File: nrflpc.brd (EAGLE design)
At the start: 67.9 x 38.8 mm, 55 parts, among them IC1 LPC1111/12/13/14-HVQFN33, IC3 LM3401, IC5 LM3401, IC6 LM3401, IC7 LM3401, IC8 78L05SMD, Q2 MOSFET-PCHANNEL, Q3 MOSFET-PCHANNEL, Q4 MOSFET-PCHANNEL, Q5 MOSFET-PCHANNEL

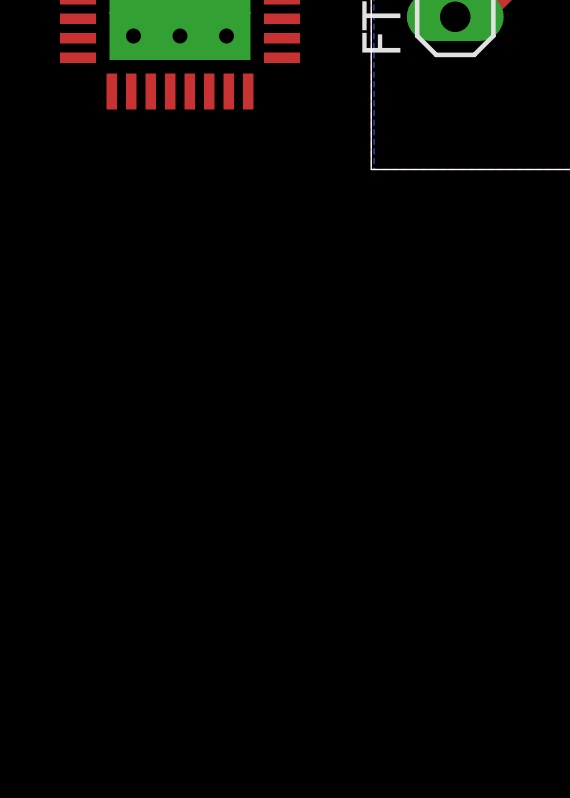
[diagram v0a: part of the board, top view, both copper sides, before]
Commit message: Basic LPC circuitry for crystal and power
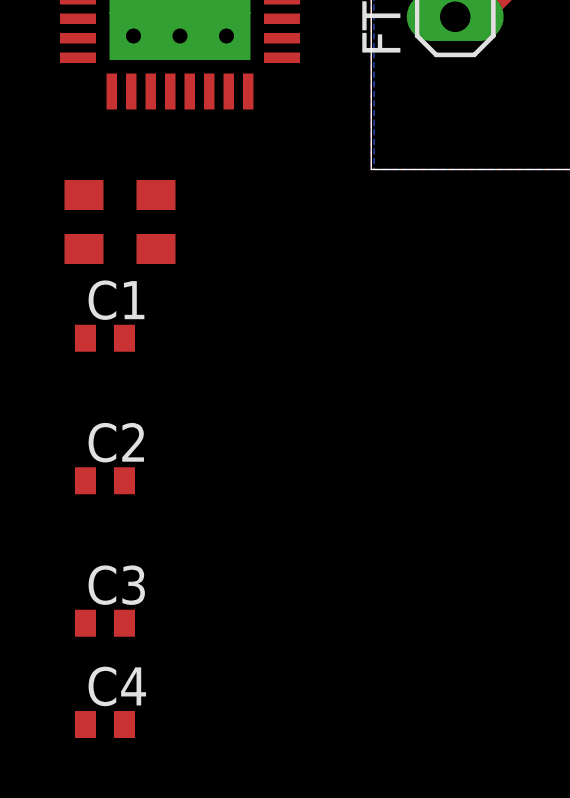
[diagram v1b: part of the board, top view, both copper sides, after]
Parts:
- added C1, C2: 18pF, rcl:C0402
- added C3, C4: 100nF, rcl:C0402
- added Q1: 20MHz, seb:MT
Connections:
- removed net VDD1: IC1.29
- removed net VDD2: IC1.6
- removed net VSS: IC1.33
- new net N$19: C2.2, IC1.4, Q1.3
- new net N$29: C1.1, IC1.5, Q1.1
- net +3V3: now also C3.1, C4.1, IC1.29, IC1.6
- net GND: now also C1.2, C2.1, C3.2, C4.2, IC1.33
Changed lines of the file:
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@@
 <element name="EXT" library="pinhead" package="2X05" value="" x="63.3" y="8.4" rot="R270"/>
 <element name="IC1" library="lpc1100v1.1" package="HVQFN33" value="LPC1111/12/13/14-HVQFN33" x="-6.375" y="6"/>
+<element name="Q1" library="seb" package="MT" value="20MHz" x="-8.375" y="-1.75"/>
+<element name="C1" library="rcl" package="C0402" value="18pF" x="-8.875" y="-5.625"/>
+<element name="C2" library="rcl" package="C0402" value="18pF" x="-8.875" y="-10.375"/>
+<element name="C3" library="rcl" package="C0402" value="100nF" x="-8.875" y="-15.125"/>
+<element name="C4" library="rcl" package="C0402" value="100nF" x="-8.875" y="-18.5"/>
 </elements>
 <signals>
@@
 <vertex x="0" y="0"/>
 </polygon>
+<contactref element="C2" pad="1"/>
+<contactref element="C1" pad="2"/>
+<contactref element="IC1" pad="33"/>
+<contactref element="C4" pad="2"/>
+<contactref element="C3" pad="2"/>
 <wire x1="52.178" y1="32.8" x2="57.66" y2="33.496" width="0" layer="19" extent="1-1"/>
 <wire x1="50.252" y1="32.743" x2="52.178" y2="32.8" width="0" layer="19" extent="1-1"/>
@@
 <wire x1="51.27" y1="3.99" x2="44" y2="6.965" width="0" layer="19" extent="1-1"/>
 <wire x1="65.052" y1="27.143" x2="57.66" y2="33.496" width="0" layer="19" extent="1-1"/>
+<wire x1="-6.375" y1="6" x2="2.8" y2="12.71" width="0" layer="19" extent="1-1"/>
+<wire x1="-8.225" y1="-5.625" x2="-6.375" y2="6" width="0" layer="19" extent="1-1"/>
+<wire x1="-9.525" y1="-10.375" x2="-8.225" y2="-5.625" width="0" layer="19" extent="1-1"/>
+<wire x1="-8.225" y1="-15.125" x2="-9.525" y2="-10.375" width="0" layer="19" extent="1-1"/>
+<wire x1="-8.225" y1="-18.5" x2="-8.225" y2="-15.125" width="0" layer="19" extent="1-1"/>
 <wire x1="64.57" y1="3.32" x2="51.27" y2="3.99" width="0" layer="19" extent="1-1"/>
 </signal>
@@
 <contactref element="JP1" pad="2"/>
 <contactref element="EXT" pad="1"/>
+<contactref element="IC1" pad="29"/>
+<contactref element="IC1" pad="6"/>
+<contactref element="C3" pad="1"/>
+<contactref element="C4" pad="1"/>
 <wire x1="48.73" y1="3.99" x2="62.03" y2="13.48" width="0" layer="19" extent="1-1"/>
 <wire x1="43.95" y1="4" x2="48.73" y2="3.99" width="0" layer="19" extent="1-1"/>
 <wire x1="44" y1="5.695" x2="43.95" y2="4" width="0" layer="19" extent="1-1"/>
+<wire x1="-6.7" y1="9.4" x2="44" y2="5.695" width="0" layer="19" extent="1-1"/>
+<wire x1="-9.775" y1="5.025" x2="-6.7" y2="9.4" width="0" layer="19" extent="1-1"/>
+<wire x1="-9.525" y1="-15.125" x2="-9.775" y2="5.025" width="0" layer="19" extent="1-1"/>
+<wire x1="-9.525" y1="-18.5" x2="-9.525" y2="-15.125" width="0" layer="19" extent="1-1"/>
 </signal>
 <signal name="CE">
@@
 <signal name="IO2">
 <contactref element="EXT" pad="9"/>
-</signal>
-<signal name="VDD1">
-<contactref element="IC1" pad="29"/>
-</signal>
-<signal name="VDD2">
-<contactref element="IC1" pad="6"/>
-</signal>
-<signal name="VSS">
-<contactref element="IC1" pad="33"/>
 </signal>
 <signal name="N$18">
@@
 <wire x1="40.7" y1="4" x2="38.8" y2="5.695" width="0" layer="19" extent="1-1"/>
 </signal>
+<signal name="N$19">
+<contactref element="IC1" pad="4"/>
+<contactref element="Q1" pad="3"/>
+<contactref element="C2" pad="2"/>
+<wire x1="-9.575" y1="-2.65" x2="-8.225" y2="-10.375" width="0" layer="19" extent="1-1"/>
+<wire x1="-9.775" y1="6.325" x2="-9.575" y2="-2.65" width="0" layer="19" extent="1-1"/>
+</signal>
+<signal name="N$29">
+<contactref element="IC1" pad="5"/>
+<contactref element="Q1" pad="1"/>
+<contactref element="C1" pad="1"/>
+<wire x1="-7.175" y1="-0.85" x2="-9.525" y2="-5.625" width="0" layer="19" extent="1-1"/>
+<wire x1="-9.775" y1="5.675" x2="-7.175" y2="-0.85" width="0" layer="19" extent="1-1"/>
+</signal>
 </signals>

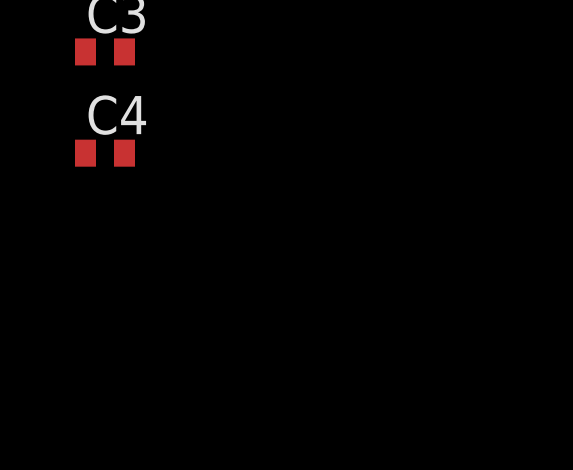
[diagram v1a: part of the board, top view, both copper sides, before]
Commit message: Chosen good fitting PWM Pins, Reset circuitry
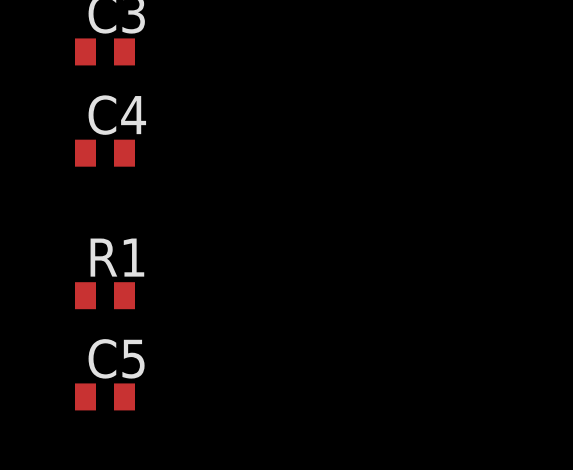
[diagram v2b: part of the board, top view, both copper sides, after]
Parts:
- added C5: 100nF, rcl:C0402
- added R1: (no value), rcl:R0402
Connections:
- net !RST: now also C5.1, IC1.2, R1.1
- net +3V3: now also R1.2
- net GND: now also C5.2
- net PB: now also IC1.25
- net PG: now also IC1.31
- net PR: now also IC1.32
- net PW: now also IC1.24
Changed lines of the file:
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@@
 <element name="C3" library="rcl" package="C0402" value="100nF" x="-8.875" y="-15.125"/>
 <element name="C4" library="rcl" package="C0402" value="100nF" x="-8.875" y="-18.5"/>
+<element name="R1" library="rcl" package="R0402" value="" x="-8.875" y="-23.25"/>
+<element name="C5" library="rcl" package="C0402" value="100nF" x="-8.875" y="-26.625"/>
 </elements>
 <signals>
@@
 <wire x1="24.25" y1="11.25" x2="25.5" y2="10" width="0.4064" layer="16"/>
 <wire x1="25.5" y1="10" x2="28.1" y2="10" width="0.4064" layer="16"/>
+<contactref element="R1" pad="1"/>
+<contactref element="C5" pad="1"/>
+<contactref element="IC1" pad="2"/>
+<wire x1="-9.525" y1="-23.25" x2="-9.525" y2="-26.625" width="0" layer="19" extent="1-1"/>
+<wire x1="-9.775" y1="7.625" x2="-9.525" y2="-23.25" width="0" layer="19" extent="1-1"/>
+<wire x1="2.8" y1="5.09" x2="-9.775" y2="7.625" width="0" layer="19" extent="1-1"/>
 </signal>
 <signal name="RXD">
@@
 <wire x1="30.3" y1="17.6" x2="35.849" y2="17.6" width="0.4064" layer="1"/>
 <wire x1="35.849" y1="17.6" x2="35.849" y2="19.0205" width="0.4064" layer="1"/>
+<contactref element="IC1" pad="25"/>
+<wire x1="-4.1" y1="9.4" x2="30.3" y2="13.0666" width="0" layer="19" extent="1-1"/>
 </signal>
 <signal name="PG">
@@
 <wire x1="19.649" y1="17.9615" x2="21.8385" y2="17.9615" width="0.4064" layer="1"/>
 <wire x1="21.8385" y1="17.9615" x2="22.2" y2="17.6" width="0.4064" layer="1"/>
+<contactref element="IC1" pad="31"/>
+<wire x1="-8" y1="9.4" x2="19.5" y2="18.1105" width="0" layer="19" extent="1-1"/>
 </signal>
 <signal name="PR">
@@
 <wire x1="5.9" y1="19.6" x2="5.9" y2="22.3" width="0.4064" layer="1"/>
 <wire x1="5.9" y1="22.3" x2="8.025" y2="24.425" width="0.4064" layer="1"/>
+<contactref element="IC1" pad="32"/>
+<wire x1="-8.65" y1="9.4" x2="5.149" y2="17.4865" width="0" layer="19" extent="1-1"/>
 </signal>
 <signal name="PW">
@@
 <wire x1="51.9" y1="16.695" x2="53.803" y2="16.695" width="0.4064" layer="1"/>
 <wire x1="53.803" y1="16.695" x2="53.803" y2="17.634" width="0.4064" layer="1"/>
+<contactref element="IC1" pad="24"/>
+<wire x1="-2.975" y1="8.275" x2="30.995" y2="16.695" width="0" layer="19" extent="1-1"/>
 </signal>
 <signal name="+12V">
@@
 <contactref element="C4" pad="2"/>
 <contactref element="C3" pad="2"/>
+<contactref element="C5" pad="2"/>
 <wire x1="52.178" y1="32.8" x2="57.66" y2="33.496" width="0" layer="19" extent="1-1"/>
 <wire x1="50.252" y1="32.743" x2="52.178" y2="32.8" width="0" layer="19" extent="1-1"/>
@@
 <wire x1="-8.225" y1="-15.125" x2="-9.525" y2="-10.375" width="0" layer="19" extent="1-1"/>
 <wire x1="-8.225" y1="-18.5" x2="-8.225" y2="-15.125" width="0" layer="19" extent="1-1"/>
+<wire x1="-8.225" y1="-26.625" x2="-8.225" y2="-18.5" width="0" layer="19" extent="1-1"/>
 <wire x1="64.57" y1="3.32" x2="51.27" y2="3.99" width="0" layer="19" extent="1-1"/>
 </signal>
@@
 <contactref element="C3" pad="1"/>
 <contactref element="C4" pad="1"/>
+<contactref element="R1" pad="2"/>
 <wire x1="48.73" y1="3.99" x2="62.03" y2="13.48" width="0" layer="19" extent="1-1"/>
 <wire x1="43.95" y1="4" x2="48.73" y2="3.99" width="0" layer="19" extent="1-1"/>
@@
 <wire x1="-9.525" y1="-15.125" x2="-9.775" y2="5.025" width="0" layer="19" extent="1-1"/>
 <wire x1="-9.525" y1="-18.5" x2="-9.525" y2="-15.125" width="0" layer="19" extent="1-1"/>
+<wire x1="-8.225" y1="-23.25" x2="-9.525" y2="-18.5" width="0" layer="19" extent="1-1"/>
 </signal>
 <signal name="CE">

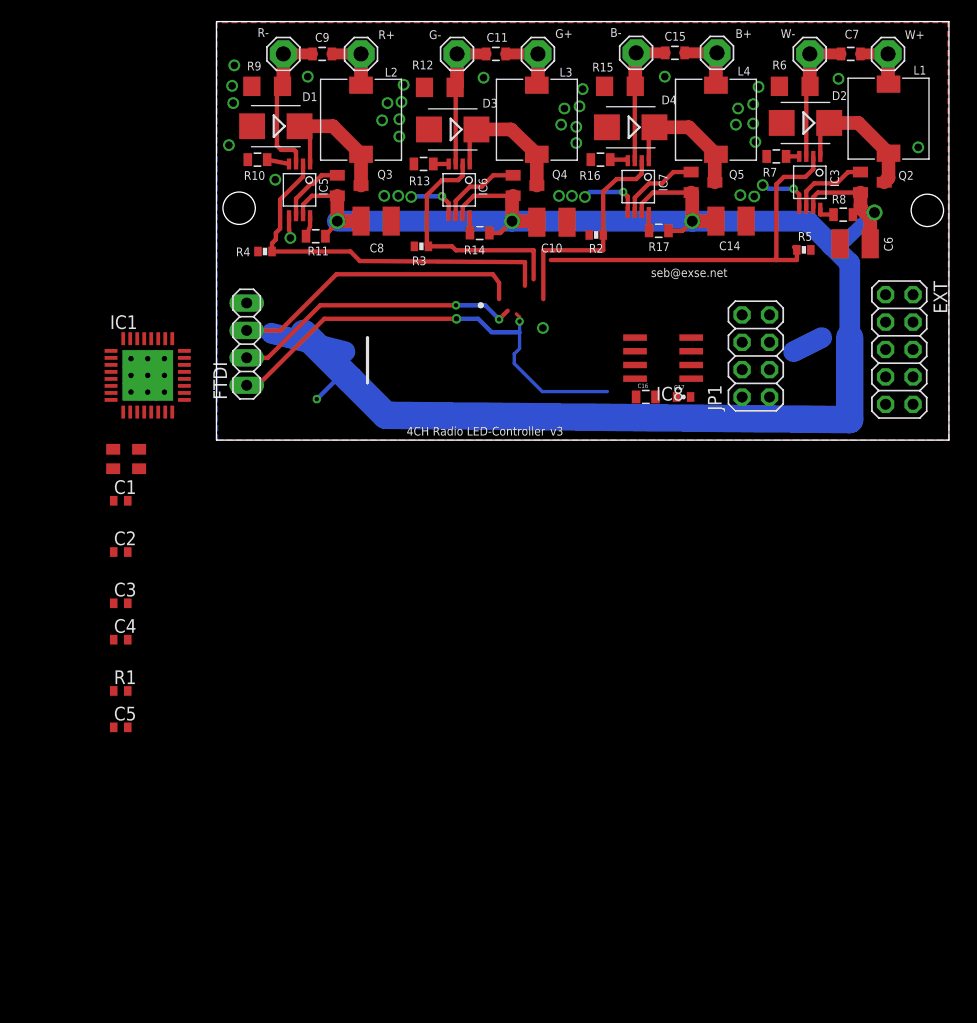
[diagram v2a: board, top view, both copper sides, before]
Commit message: Mostly final signal assignment, Starting to place
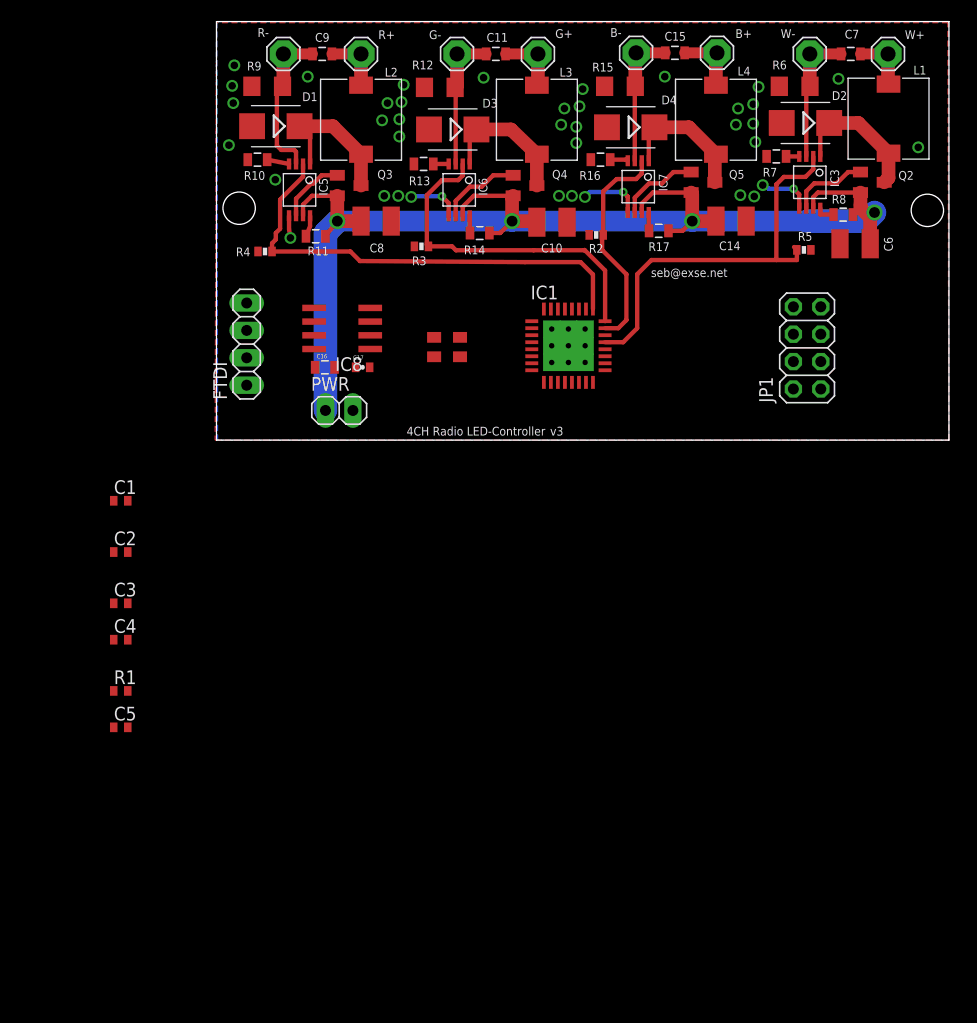
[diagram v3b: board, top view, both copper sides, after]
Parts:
- removed EXT: (no value), pinhead:2X05
- added PWR: (no value), pinhead:1X02
- moved IC1 39.1 mm to (32.6, 8.75)
- moved Q1 31.5 mm to (21.4, 8.62)
- moved IC8 29.9 mm to (11.7, 10.3)
- moved C16 29.9 mm to (10.1, 6.75)
- moved C17 29.9 mm to (13.6, 6.75)
- moved JP1 4.81 mm to (54.8, 8.55)
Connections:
- removed net +5V: EXT.2
- removed net AIN0: EXT.5
- removed net AIN1: EXT.6
- removed net INT: EXT.3
- new net AD0: IC1.20
- new net AD1: IC1.22
- net +12V: now also PWR.1; no longer EXT.4
- net +3V3: no longer EXT.1
- net CE: now also IC1.14
- net CSN: now also IC1.16
- net GND: now also PWR.2; no longer EXT.10
- net IO0: now also IC1.9; no longer EXT.7
- net IO1: now also IC1.10; no longer EXT.8
- net IO2: now also IC1.11; no longer EXT.9
- net IRQ: now also IC1.15
- net MISO: now also IC1.17
- net MOSI: now also IC1.18
- net PB: now also IC1.23; no longer IC1.25
- net PG: now also IC1.24; no longer IC1.31
- net PR: now also IC1.25; no longer IC1.32
- net PW: now also IC1.21; no longer IC1.24
- net RXD: now also IC1.31
- net SCK: now also IC1.19
- net TXD: now also IC1.32
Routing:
- net +12V: track 176.3 -> 118.1 mm, vias 5 -> 4
- net !RST: track 43.0 -> 1.04 mm, vias 2 -> 0
- net TXD: track 27.5 -> 0.00 mm
- net RXD: track 27.1 -> 0.00 mm, vias 2 -> 0
- net PG: track 22.6 -> 32.0 mm
- net PR: track 35.3 -> 43.1 mm
- net N$27: track 7.01 -> 0.00 mm
- net N$28: track 2.91 -> 0.00 mm
- net PW: track 36.3 -> 37.4 mm
- net GND: vias 42 -> 41
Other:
- board text removed: "C1"
- board text removed: "C12"
- board text removed: "C13"
- board text removed: "C2"
- board text removed: "C3"
- board text removed: "C4"
- board text removed: "C5"
- board text removed: "IC1"
- board text removed: "IC4"
- board text removed: "ISP"
- board text removed: "Q1"
- board text removed: "R1"
